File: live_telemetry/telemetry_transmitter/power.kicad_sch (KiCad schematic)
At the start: 14 parts, among them J3 BUS_CONN

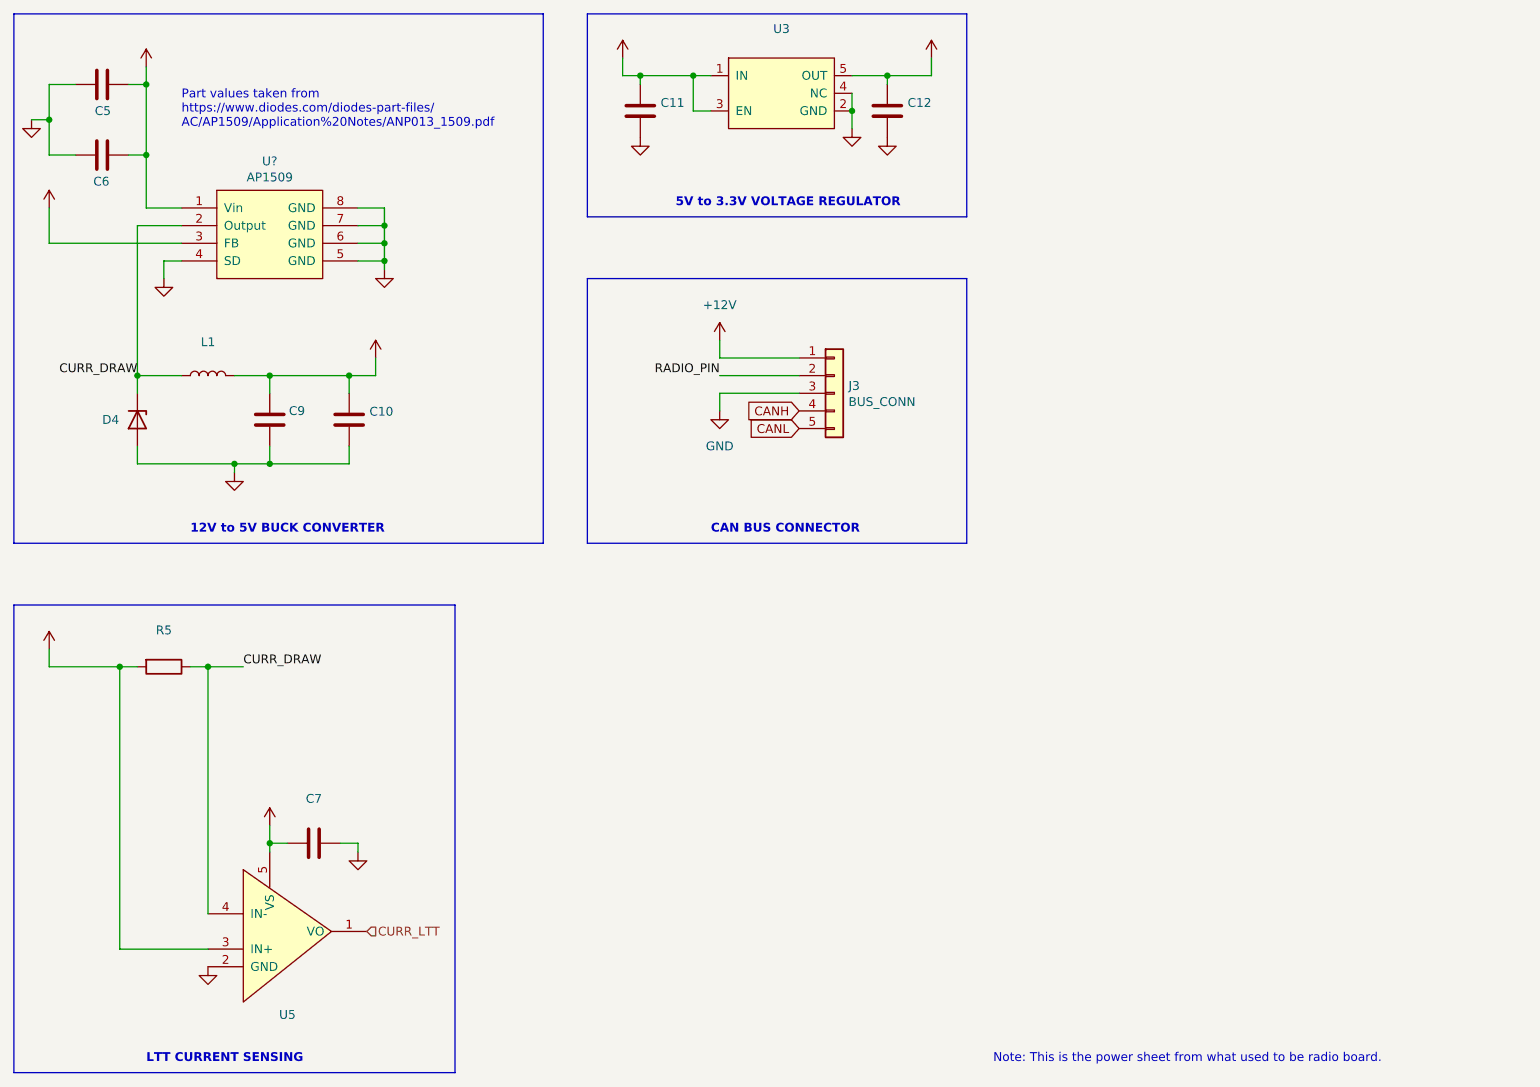
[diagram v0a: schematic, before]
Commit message: added dual diode to control board reset with radio gpio
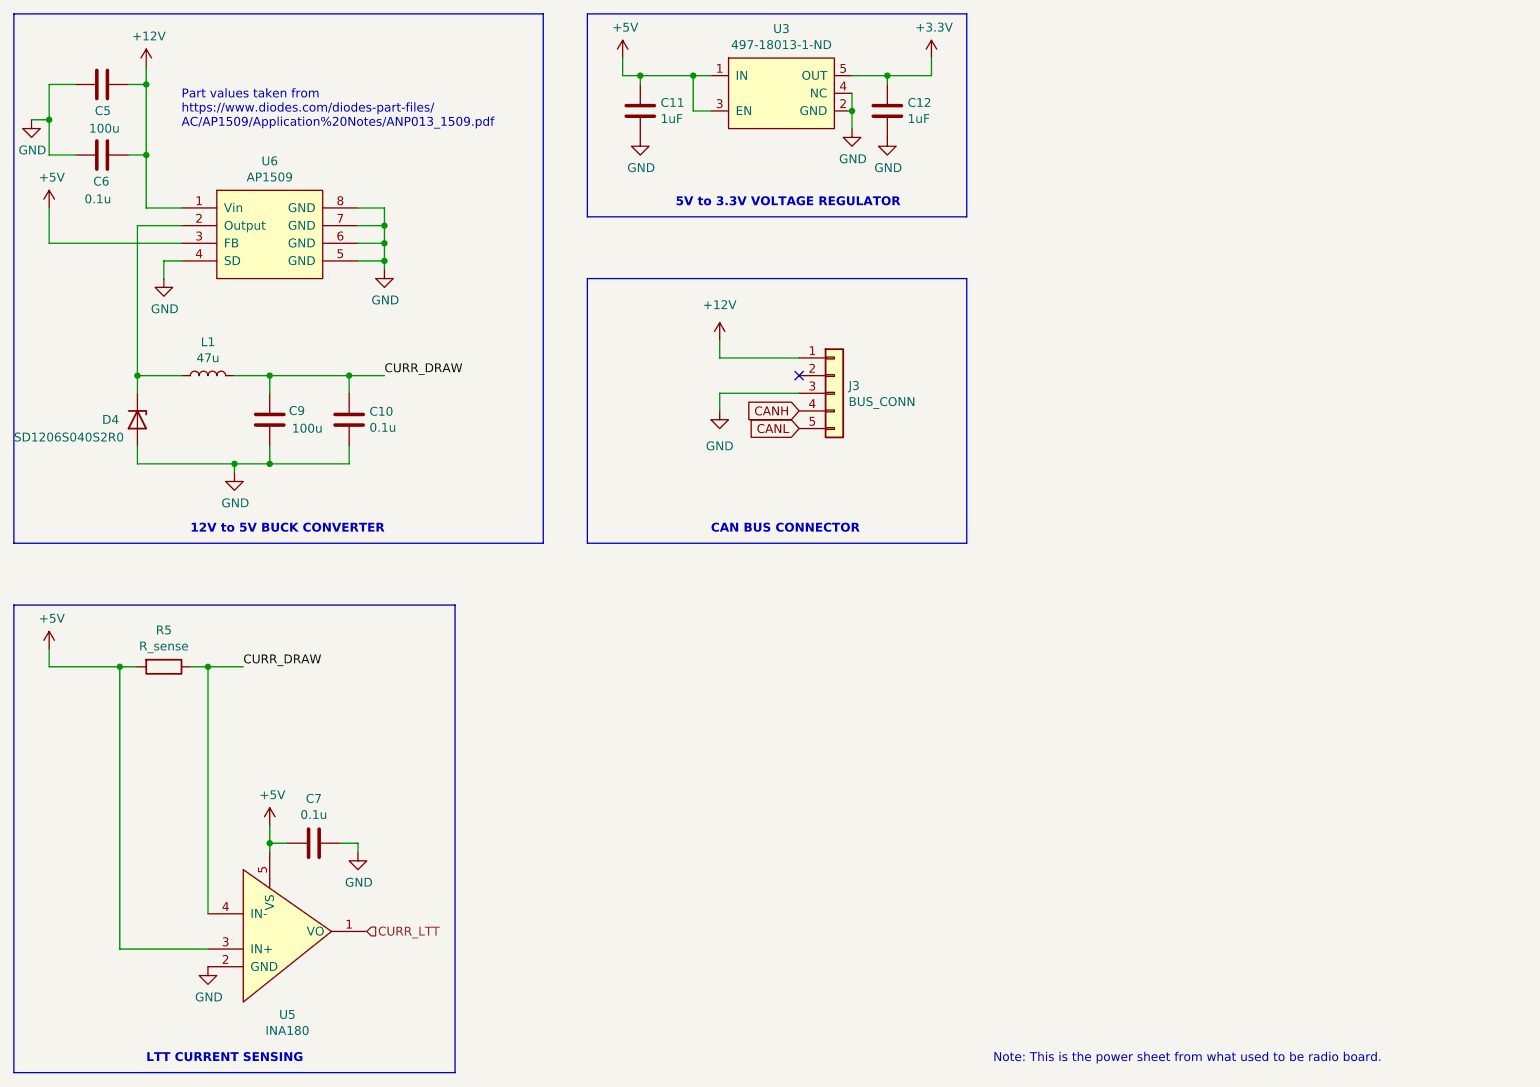
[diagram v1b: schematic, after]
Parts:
- C10, C6, C7: value (none) -> 0.1u; footprint (none) -> Capacitor_SMD:C_0805_2012Metric_Pad1.15x1.40mm_HandSolder
- C11, C12: value (none) -> 1uF; footprint (none) -> Capacitor_SMD:C_0805_2012Metric_Pad1.15x1.40mm_HandSolder
- C5, C9: value (none) -> 100u; footprint (none) -> Capacitor_THT:CP_Radial_D7.5mm_P2.50mm
- D4: value (none) -> SD1206S040S2R0; footprint (none) -> Diode_SMD:D_1206_3216Metric_Pad1.42x1.75mm_HandSolder
- L1: value (none) -> 47u; footprint (none) -> Inductor_THT:L_Radial_D8.7mm_P5.00mm_Fastron_07HCP
- R5: value (none) -> R_sense; footprint (none) -> Resistor_SMD:R_1206_3216Metric_Pad1.42x1.75mm_HandSolder
- U3: value (none) -> 497-18013-1-ND; footprint (none) -> Package_TO_SOT_SMD:SOT-23-5_HandSoldering
- U5: value (none) -> INA180; footprint (none) -> Package_TO_SOT_SMD:SOT-23-5_HandSoldering
- gave numbers to parts that had none: 1
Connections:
- net +5V: no longer C10.2, C9.1, L1.2
- net CURR_DRAW: now also C10.2, C9.1, L1.2; no longer D4.1 (K), L1.1, U6.2 (Output)
- net RADIO_PIN: no longer names the net of J3.2 (Pin_2)
- new net: D4.1 (K), L1.1, U6.2 (Output)
- no-connect marks 0 -> 1

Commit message: Addressed comments, radio pinout looks ok will double check in person tomorrow
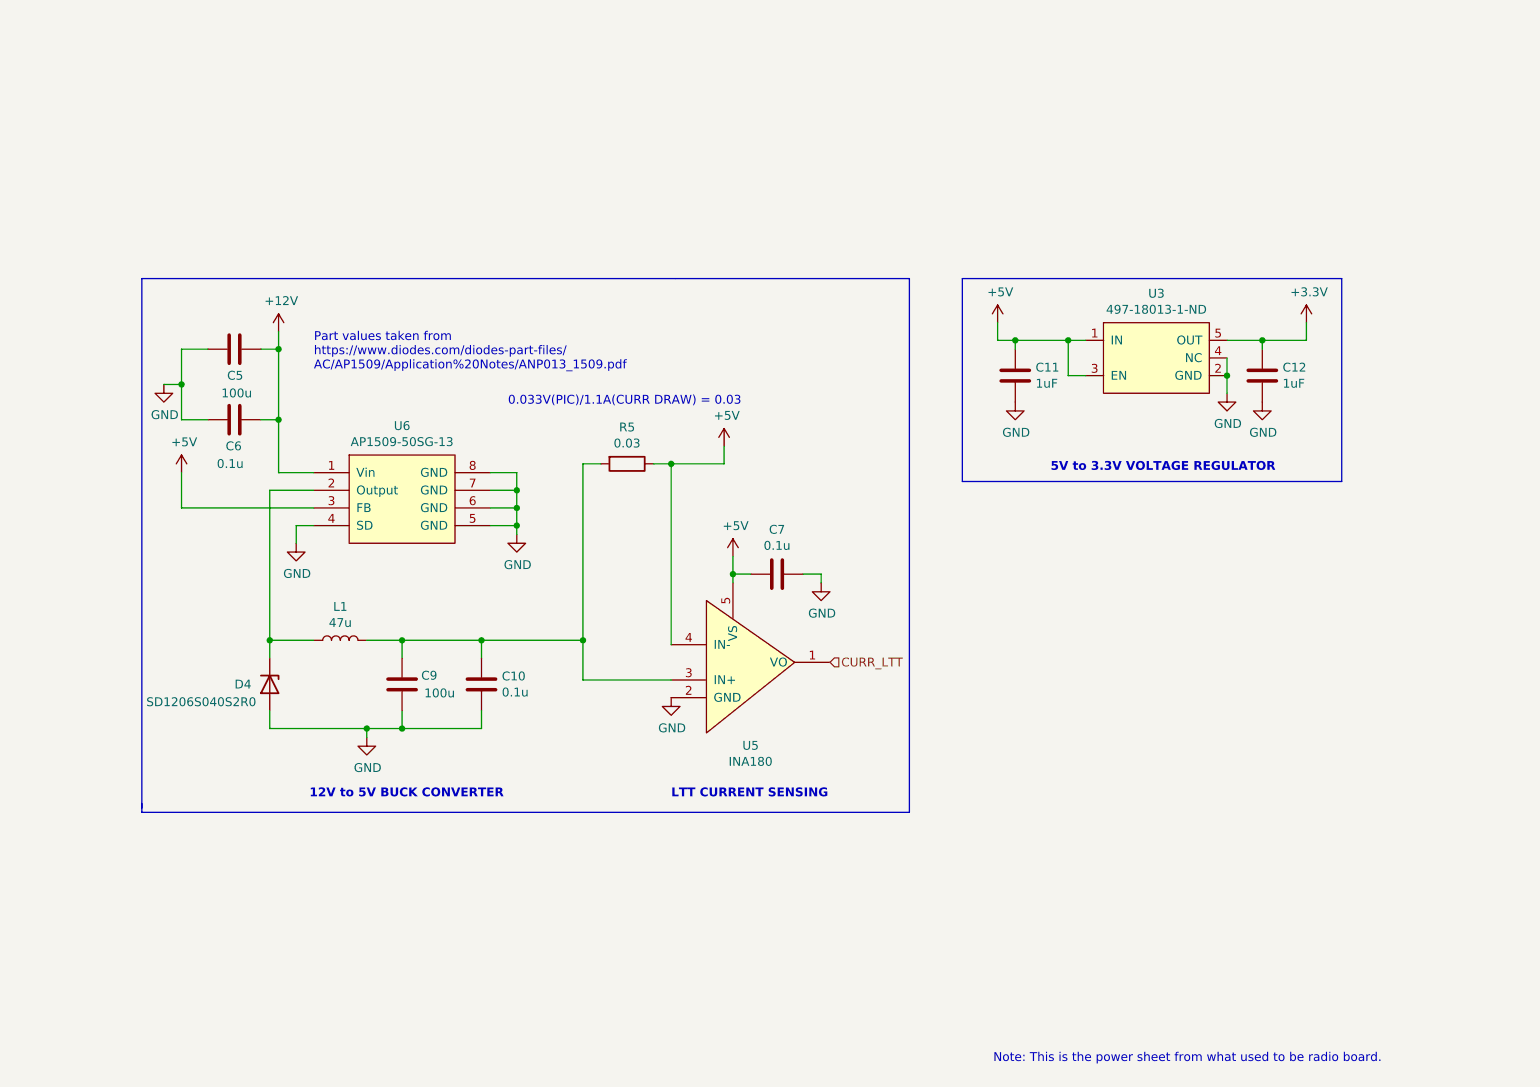
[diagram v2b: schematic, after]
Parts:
- removed J3: BUS_CONN, canhw_footprints:connector_Harwin_M80-5000642, symbol Connector_Generic:Conn_01x05
- R5: value R_sense -> 0.03
- U6: value AP1509 -> AP1509-50SG-13
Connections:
- net +5V: now also R5.1, U5.4 (IN-); no longer R5.2, U5.3 (IN+)
- net CURR_DRAW: no longer names the net of C10.2, C9.1, L1.2
- net CURR_DRAW: now also R5.2, U5.3 (IN+); no longer R5.1, U5.4 (IN-)
- no-connect marks 1 -> 0
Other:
- note added: "0.033V(PIC)/1.1A(CURR DRAW) = 0.03"
- note removed: "CAN BUS CONNECTOR"
- moved on the sheet: C10, C11, C12, C5, C6, C7, C9, D4, L1, R5, U3, U5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

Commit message: Addressed comments
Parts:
- R5: value 0.03 -> 0.02R
- U3: value 497-18013-1-ND -> LDLN030G33R
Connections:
- net +5V: no longer C7.2, U5.5 (VS)
- net GND: no longer U3.4 (NC)
- new net: C7.2, U5.5 (VS)
- no-connect marks 0 -> 1
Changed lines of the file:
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@@
   (junction (at 90.17 127) (diameter 0) (color 0 0 0 0)
   )
-  (junction (at 213.995 76.2) (diameter 0) (color 0 0 0 0)
-  )
   (junction (at 191.135 71.12) (diameter 0) (color 0 0 0 0)
   )
@@
   (junction (at 95.25 127) (diameter 0) (color 0 0 0 0)
   )
+  (no_connect (at 213.995 73.66))
   (polyline (pts (xy 175.895 91.44) (xy 230.505 91.44))
     (stroke (width 0) (type default) (color 0 0 0 0))
@@
   )
   (wire (pts (xy 95.25 114.3) (xy 106.68 114.3))
-    (stroke (width 0) (type default) (color 0 0 0 0))
-  )
-  (wire (pts (xy 213.995 73.66) (xy 213.995 76.2))
     (stroke (width 0) (type default) (color 0 0 0 0))
   )
@@
     (in_bom yes) (on_board yes)
     (property "Reference" "R5" (id 0) (at 127.635 83.6422 90))
-    (property "Value" "0.03" (id 1) (at 127.635 85.9536 90))
+    (property "Value" "0.02R" (id 1) (at 127.635 85.9536 90))
     (property "Footprint" "Resistor_SMD:R_1206_3216Metric_Pad1.42x1.75mm_HandSolder" (id 2) (at 127.635 87.122 90)
       (effects (font (size 1.27 1.27)) hide)
@@
     )
     (property "Datasheet" "" (id 3) (at 155.575 106.045 0)
-      (effects (font (size 1.27 1.27)) hide)
-    )
-    (pin "1")
-  )
-  (symbol (lib_id "power:+5V") (at 142.875 102.235 0) (unit 1)
-    (in_bom yes) (on_board yes)
-    (property "Reference" "#PWR017" (id 0) (at 142.875 106.045 0)
-      (effects (font (size 1.27 1.27)) hide)
-    )
-    (property "Value" "+5V" (id 1) (at 143.256 97.8408 0))
-    (property "Footprint" "" (id 2) (at 142.875 102.235 0)
-      (effects (font (size 1.27 1.27)) hide)
-    )
-    (property "Datasheet" "" (id 3) (at 142.875 102.235 0)
       (effects (font (size 1.27 1.27)) hide)
     )
@@
     (in_bom yes) (on_board yes)
     (property "Reference" "U3" (id 0) (at 203.835 64.389 0))
-    (property "Value" "497-18013-1-ND" (id 1) (at 203.835 66.7004 0))
+    (property "Value" "LDLN030G33R" (id 1) (at 203.835 66.7004 0))
     (property "Footprint" "Package_TO_SOT_SMD:SOT-23-5_HandSoldering" (id 2) (at 203.835 81.28 0)
       (effects (font (size 1.27 1.27)) hide)
@@
   (symbol (lib_id "power:+5V") (at 141.605 86.36 0) (unit 1)
     (in_bom yes) (on_board yes)
-    (property "Reference" "#PWR?" (id 0) (at 141.605 90.17 0)
-      (effects (font (size 1.27 1.27)) hide)
-    )
+    (property "Reference" "#PWR022" (id 0) (at 141.605 90.17 0)
+      (effects (font (size 1.27 1.27)) hide)
+    )

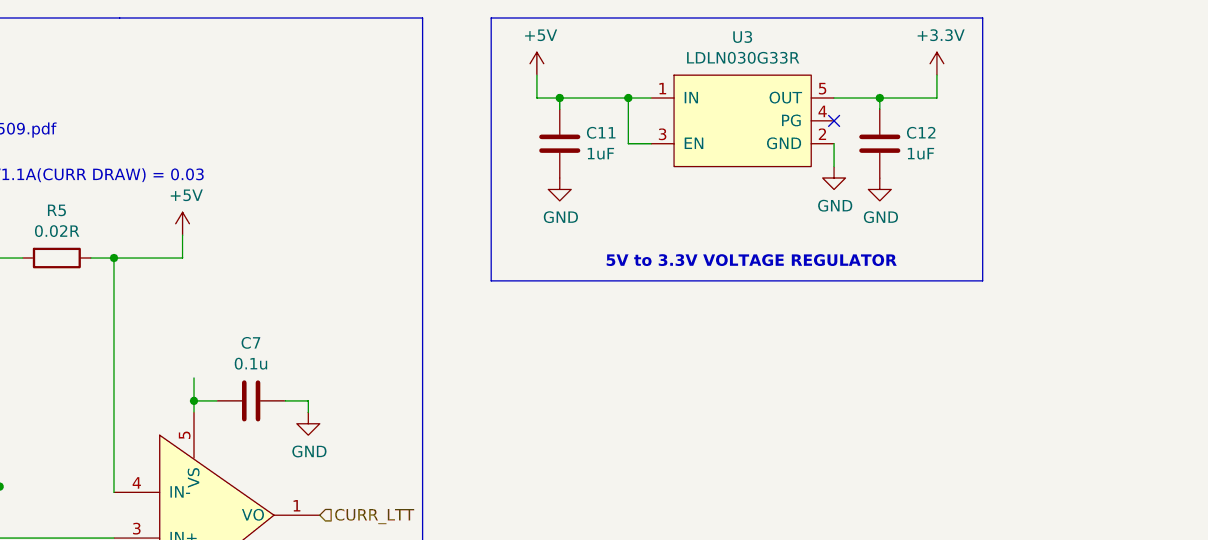
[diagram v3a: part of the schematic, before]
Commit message: Addressed remaining comments, unsure about caps for U3. Datasheet was unclear
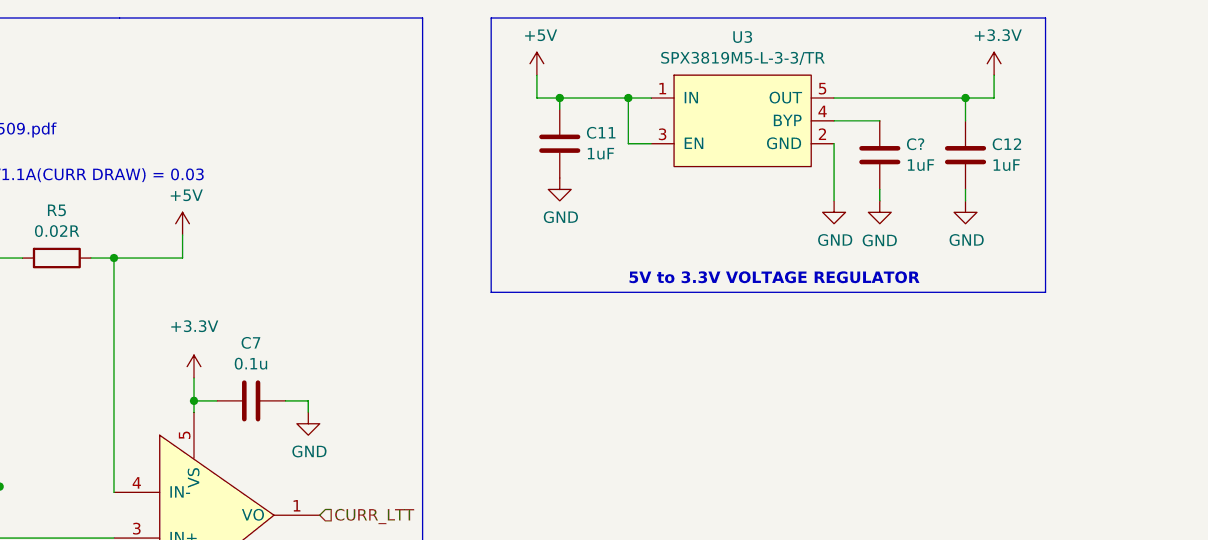
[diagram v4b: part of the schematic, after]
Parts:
- added C?: 1uF, Capacitor_SMD:C_0805_2012Metric_Pad1.15x1.40mm_HandSolder, symbol Device:C
- U3: value LDLN030G33R -> SPX3819M5-L-3-3/TR
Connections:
- net GND: now also C?.1
- net +3.3V: now reaches C7.2, U5.5 (VS)
- net at U3.4 (BYP): now also C?.2
- no-connect marks 1 -> 0
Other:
- moved on the sheet: C12
